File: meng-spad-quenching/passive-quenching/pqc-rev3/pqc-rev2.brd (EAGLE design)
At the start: 38.1 x 25.4 mm, 54 parts, among them IC1 OPA858, IC2 OPA858, IC3 LM8261, IC4 TPS7A4901, Q1 NTR5105P, Q2 BSS123LT1G, Q3 NUD3160LT1G, X1 CONN_SPAD, X2 VIN_PWR, X4 VIN_BIAS, X5 SIGNAL_OUT

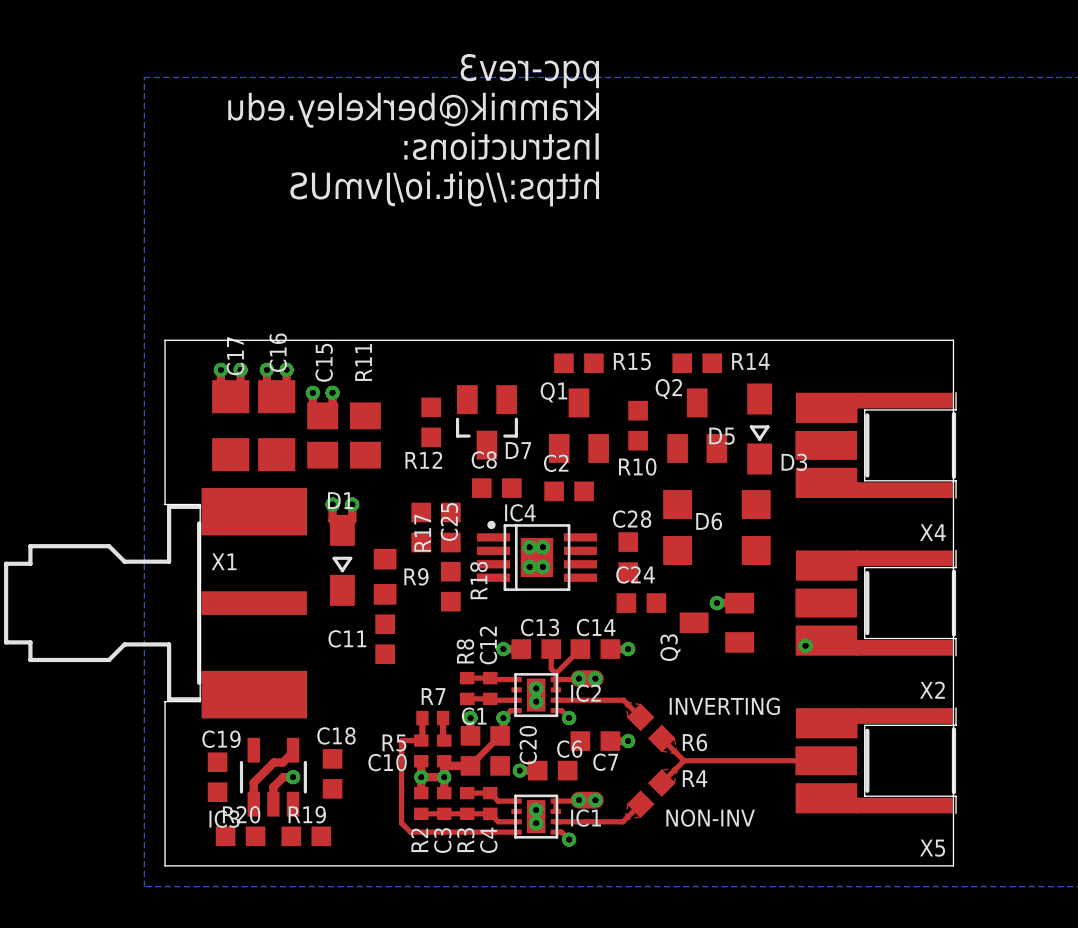
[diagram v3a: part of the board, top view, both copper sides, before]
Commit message: Finished layout, renumbered, and exported Gerbers
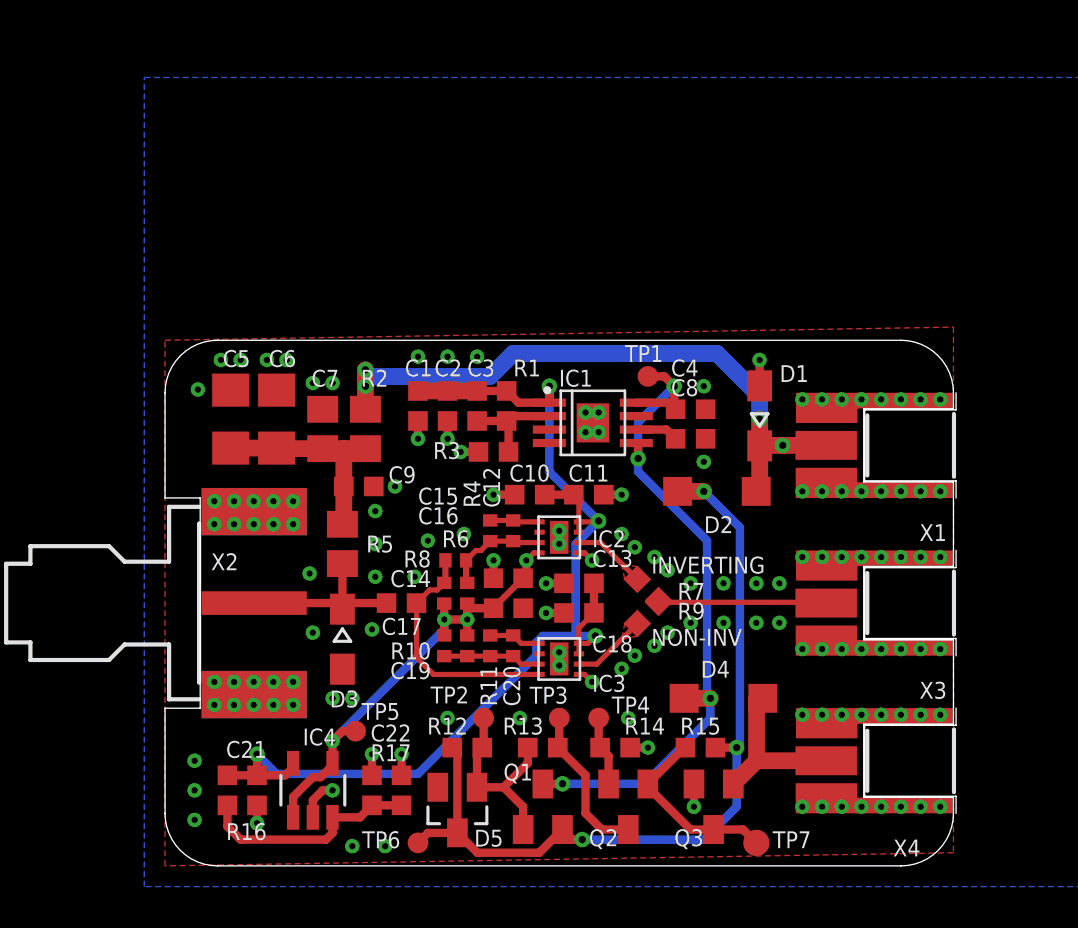
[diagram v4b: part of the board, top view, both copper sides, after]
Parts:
- removed C24, C25: CAP CER 10000PF 25V X7R 0603 10%, rcl-modified-footprints:C0603
- removed C28: CAP CER 0.1UF 100V X7R 0603, rcl-modified-footprints:C0603
- removed D6: MMSD4148, diode:SOD123
- removed D7: BZX84C6V2L, diode:SOT23
- removed R18: RES SMD 24K OHM 1% 1/10W 0603, rcl-modified-footprints:R0603
- removed R19, R20: RES SMD 1K OHM 1% 1/10W 0603, rcl-modified-footprints:R0603
- removed X5: SIGNAL_OUT, con-samtec:MMCX-J-P-X-ST-EM1-MKT
- added C21, C22: CAP CER 0.1UF 100V X7R 0603, rcl-modified-footprints:C0603
- added C5: CAP CER 10UF 50V X5R 1206, rcl:C1206
- added C9: CAP CER 10NF 50V X7R 0603, rcl-modified-footprints:C0603
- added D2, D4: MMSD4148, diode:SOD123
- added R1: RES SMD 76.8K OHM 1% 1/10W 0603, rcl-modified-footprints:R0603
- added R13: RES SMD 10K OHM 1% 1/10W 0603, rcl-modified-footprints:R0603
- added R16: RES SMD 1K OHM 1% 1/10W 0603, rcl-modified-footprints:R0603
- added TP1, TP2, TP3, TP4, TP5, TP6: TPTP10R, testpad:TP10R
- added TP7: TPB1,27, testpad:B1,27
- added X3: SIGNAL_OUT, con-samtec:MMCX-J-P-X-ST-EM1-MKT
- C1: value CAP CER 10000PF 25V C0G 0603 -> CAP CER 10UF 10V X5R 0603
- C10: value C_TUNE2 -> CAP CER 10000PF 25V C0G 0603; device rcl-modified-footprints:C0402 -> rcl-modified-footprints:C0603
- C11: value C_SNS -> CAP CER 0.1UF 25V X7R 0603
- C13: value CAP CER 10000PF 25V C0G 0603 -> CAP CER 0.1UF 25V X7R 0603
- C14: value CAP CER 0.1UF 25V X7R 0603 -> C_TUNE2; device rcl-modified-footprints:C0603 -> rcl-modified-footprints:C0402
- C15: value CAP CER 0.1UF 16V X7R 0805 -> CAP CER 10000PF 25V C0G 0603; device rcl:C0805 -> rcl-modified-footprints:C0603
- C16: value CAP CER 1UF 16V X7R 1206 -> CAP CER 0.1UF 100V X7R 0603; device rcl:C1206 -> rcl-modified-footprints:C0603
- C17: value CAP CER 10UF 16V X7R 1206 -> C_SNS; device rcl:C1206 -> rcl-modified-footprints:C0603
- C18: value CAP CER 0.1UF 100V X7R 0603 -> CAP CER 10000PF 25V C0G 0603
- C19: value CAP CER 0.1UF 100V X7R 0603 -> C_FB2; device rcl-modified-footprints:C0603 -> rcl-modified-footprints:C0402
- C20: value CAP CER 0.1UF 100V X7R 0603 -> C_FB1; device rcl-modified-footprints:C0603 -> rcl-modified-footprints:C0402
- C3: value C_FB2 -> CAP CER 10000PF 25V X7R 0603 10%; device rcl-modified-footprints:C0402 -> rcl-modified-footprints:C0603
- C4: value C_FB1 -> CAP CER 0.1UF 100V X7R 0603; device rcl-modified-footprints:C0402 -> rcl-modified-footprints:C0603
- C6: value CAP CER 10000PF 25V C0G 0603 -> CAP CER 1UF 50V X7R 1206; device rcl-modified-footprints:C0603 -> rcl:C1206
- C7: value CAP CER 0.1UF 25V X7R 0603 -> CAP CER 0.1UF 50V X7R 0805; device rcl-modified-footprints:C0603 -> rcl:C0805
- C8: value CAP CER 10UF 10V X5R 0603 -> CAP CER 10000PF 25V X7R 0603 10%
- D5: value MMSD4148 -> BZX84C6V2L; device diode:SOD123 -> diode:SOT23
- IC1: value OPA858 -> TPS7A4901; device meng:WSON8 -> Kramnik's Library:MSOP-8_POWER_PAD
- IC3: value LM8261 -> OPA858; device meng:SOT23-5 -> meng:WSON8
- IC4: value TPS7A4901 -> LM8261; device Kramnik's Library:MSOP-8_POWER_PAD -> meng:SOT23-5
- R10: value RES SMD 10M OHM 1% 1/10W 0603 -> R_FB2; device rcl-modified-footprints:R0603 -> rcl-modified-footprints:R0402
- R11: value RES SMD 1 OHM 1% 0805 -> R_FB1; device rcl:R0805 -> rcl-modified-footprints:R0402
- R15: value RES SMD 10K OHM 1% 1/10W 0603 -> RES SMD 10M OHM 1% 1/10W 0603
- R17: value RES SMD 76.8K OHM 1% 1/10W 0603 -> RES SMD 1K OHM 1% 1/10W 0603
- R2: value R_FB2 -> RES SMD 1 OHM 1% 0805; device rcl-modified-footprints:R0402 -> rcl:R0805
- R3: value R_FB1 -> RES SMD 24K OHM 1% 1/10W 0603; device rcl-modified-footprints:R0402 -> rcl-modified-footprints:R0603
- R4: value RES SMD 50 OHM 1% 0603 -> R_TIA; device rcl-modified-footprints:R0603 -> rcl-modified-footprints:R0402
- R5: value R_SNS -> R_Q; device rcl-modified-footprints:R0402 -> rcl:R0805
- R6: value RES SMD 50 OHM 1% 0603 -> R_SNS1; device rcl-modified-footprints:R0603 -> rcl-modified-footprints:R0402
- R7: value R_SNS1 -> RES SMD 50 OHM 1% 0603; device rcl-modified-footprints:R0402 -> rcl-modified-footprints:R0603
- R8: value R_TIA -> R_SNS
- R9: value R_Q -> RES SMD 50 OHM 1% 0603; device rcl:R0603 -> rcl-modified-footprints:R0603
- X1: value CONN_SPAD -> VIN_BIAS; device meng:J502-ND-142-0701-881/886 -> con-samtec:MMCX-J-P-X-ST-EM1-MKT
- X2: value VIN_PWR -> SPAD; device con-samtec:MMCX-J-P-X-ST-EM1-MKT -> meng:J502-ND-142-0701-881/886
- X4: value VIN_BIAS -> VIN_PWR
- moved X1 37.1 mm to (38.1, 20.3), turned to 270 degrees
- moved X2 36.4 mm to (1.75, 12.7), turned to 0 degrees
- moved D3 22.6 mm to (8.57, 11.0), turned to 270 degrees
- moved C6 21.6 mm to (5.40, 21.6), turned to 90 degrees
- moved C4 21.4 mm to (25.4, 22.1), turned to 0 degrees
- moved D1 21.3 mm to (28.7, 21.7)
- moved C7 20.0 mm to (7.62, 21.1), turned to 90 degrees
- moved IC1 20.0 mm to (18.6, 22.4), turned to 270 degrees
- moved R15 19.5 mm to (25.9, 5.71), turned to 0 degrees
- moved D5 19.4 mm to (14.1, 2.70), turned to 180 degrees
- moved C3 19.3 mm to (15.1, 22.2), turned to 270 degrees
- moved R14 19.0 mm to (21.7, 5.71), turned to 180 degrees
- moved Q2 18.7 mm to (22.4, 2.86), turned to 180 degrees
- moved Q1 18.5 mm to (18.3, 2.86)
- moved R2 18.3 mm to (9.68, 21.1)
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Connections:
- removed net N$1: C15.1, C16.1, C17.1, R11.1, R9.2
- removed net N$10: C3.1, C4.2, IC1.3, R2.1, R3.2
- removed net N$11: C4.1, IC1.1, R3.1
- removed net N$12: R4.1, R6.1, X5.1
- removed net N$16: IC1.6, R4.2
- removed net N$2: C11.1, D1.C, R9.1, X1.1
- removed net N$4: C10.1, C12.2, IC2.3, R7.1, R8.2
- removed net N$5: C12.1, IC2.1, R8.1
- removed net N$6: C11.2, IC1.4, R5.2, R7.2
- removed net N$7: IC2.6, R6.2
- new net INV_FB: C12.1, IC2.1, R4.1
- new net INV_IN_M: C12.2, C14.1, IC2.3, R4.2, R6.1
- new net INV_OUT: IC2.6, R7.2
- new net NON_INV_FB: C20.1, IC3.1, R11.1
- new net NON_INV_IN_M: C19.1, C20.2, IC3.3, R10.1, R11.2
- new net NON_INV_OUT: IC3.6, R9.2
- new net RSENSE_NODE: C17.2, IC3.4, R6.2, R8.2
- new net SIGNAL_OUT: R7.1, R9.1, X3.1
- new net SPAD_KATHODE: C17.1, D3.C, R5.1, X2.1
- new net VBIAS_IN_R: C5.1, C6.1, C7.1, C9.1, R2.1, R5.2
- net GND: now also C10.2, C11.2, C21.2, C22.2, C4.2, C5.2, C9.2, IC1.4, IC3.5, IC3.PAD, IC4.2, R17.1, R3.2, X1.2@1, X1.2@2, X1.2@3, X1.2@4, X2.G@1, X2.G@2, X2.G@3, X2.G@4, X3.2@1, X3.2@2, X3.2@3, X3.2@4; no longer C14.2, C17.2, C19.2, C20.2, C24.2, C28.2, IC1.5, IC3.2, IC4.4, IC4.PAD, R18.2, R20.1, X1.G@1, X1.G@2, X1.G@3, X1.G@4, X2.2@1, X2.2@2, X2.2@3, X2.2@4, X5.2@1, X5.2@2, X5.2@3, X5.2@4
- net LDO_FB: now also C3.2, IC1.2, R1.1, R3.1; no longer C25.2, IC4.2, R17.1, R18.1
- net LDO_IN: now also C4.1, D4.C, IC1.5, IC1.8, TP1.TP; no longer C28.1, D6.C, IC4.5, IC4.8
- net LDO_P5V0_NR_SS_CH1: now also C8.1, IC1.6; no longer C24.1, IC4.6
- net LOAD_SW_NMOS_DRAIN: now also R13.1, TP3.TP; no longer R15.1
- net LOAD_SW_NMOS_GATE: now also R15.1, TP7.TP; no longer R10.1
- net LOAD_SW_NMOS_SOURCE: now also TP4.TP
- net LOAD_SW_PMOS_GATE: now also D5.1, R13.2, TP2.TP; no longer D7.1, R15.2
- net LOAD_SW_PMOS_SOURCE: now also D2.C, D5.3, R15.2, TP6.TP; no longer D5.C, D7.3, R10.2
- net PP_P5V0_ANALOG: now also C1.1, C10.1, C11.1, C18.1, C21.1, C3.1, IC1.1, IC3.7, IC3.8, IC4.5, R1.2, R16.2; no longer C14.1, C19.1, C25.1, C6.1, C7.1, C8.1, IC1.7, IC1.8, IC3.5, IC4.1, R17.2, R19.2
- net VBIAS_IN: now also D1.C, D2.A, R2.2, X1.1; no longer D3.C, D5.A, R11.2, X4.1
- net VPWR_IN: now also D4.A, X4.1; no longer D6.A, X2.1
- net VREF_2V5: now also C14.2, C15.1, C16.1, C19.2, IC4.1, IC4.4, R10.2, R8.1, TP5.TP; no longer C1.1, C10.2, C20.1, C3.2, IC3.1, IC3.4, R2.2, R5.1
- net VREF_DIVIDER: now also C22.1, IC4.3, R16.1, R17.2; no longer C18.1, IC3.3, R19.1, R20.2
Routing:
- net PP_P5V0_ANALOG: track 9.68 -> 54.4 mm
- net LOAD_SW_PMOS_SOURCE: track 0.00 -> 39.9 mm, vias 0 -> 3
- net LDO_IN: track 0.00 -> 34.3 mm, vias 0 -> 4
- net VBIAS_IN: track 0.00 -> 31.0 mm, vias 0 -> 4
- net VREF_2V5: track 12.9 -> 24.8 mm, vias 3 -> 4
- net N$6: track 11.8 -> 0.00 mm
- net RSENSE_NODE: track 0.00 -> 11.8 mm
- net VREF_DIVIDER: track 0.00 -> 10.8 mm
- net VBIAS_IN_R: track 0.00 -> 10.3 mm
- net N$12: track 9.91 -> 0.00 mm
- net LOAD_SW_PMOS_GATE: track 0.00 -> 9.59 mm
- net LOAD_SW_NMOS_GATE: track 0.00 -> 9.05 mm
- net SPAD_KATHODE: track 0.00 -> 8.60 mm
- net SIGNAL_OUT: track 0.00 -> 8.38 mm
- net VPWR_IN: track 0.00 -> 8.27 mm
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- added copper zone on layer 1, net GND
- added copper zone on layer 15, net GND
- added copper zone on layer 1, net INV_OUT
- added copper zone on layer 1, net NON_INV_OUT
- removed copper zone on layer 1, net N$12
- removed copper zone on layer 1, net N$16
- removed copper zone on layer 1, net N$7
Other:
- outline, holes or cut-outs redrawn
